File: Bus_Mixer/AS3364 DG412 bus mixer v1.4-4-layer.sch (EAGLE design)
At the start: 139 parts, among them IC1 PCA9539PW, IC10 DG412-J, IC11 DG412-J, IC2 TL074JT, IC3 TL072JT, IC4 TL074JT, IC6 TL072JT, IC7 TL074JT, IC8 DG412-J, IC9 DG412-J

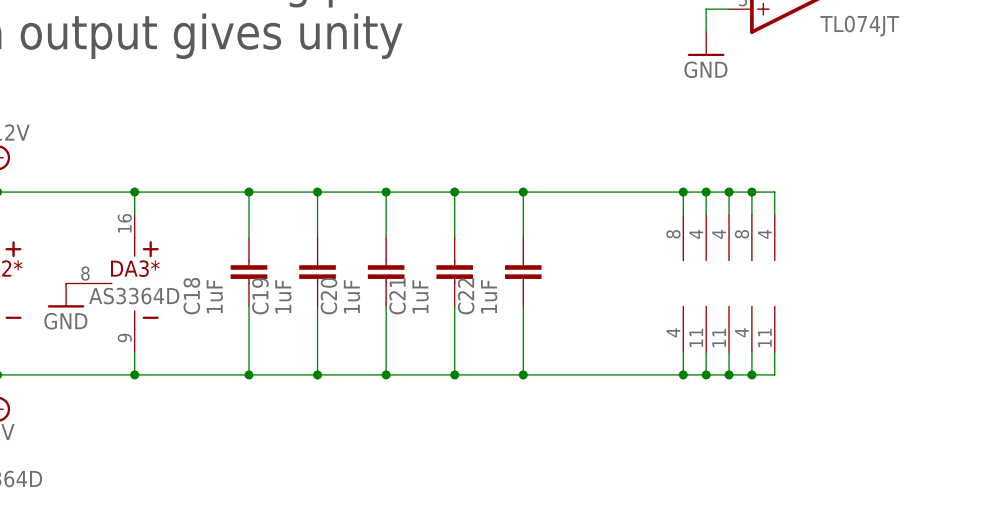
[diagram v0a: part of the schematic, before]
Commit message: Added better decoupling caps
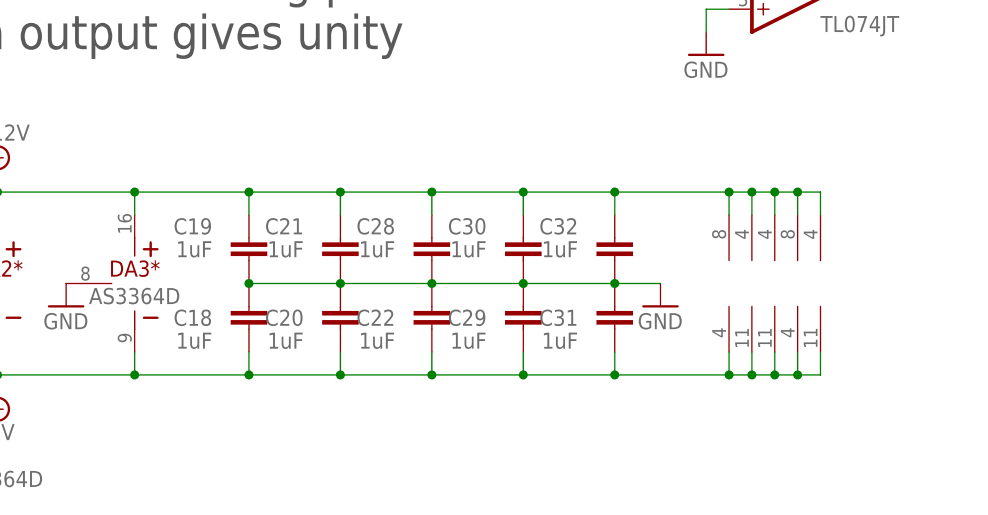
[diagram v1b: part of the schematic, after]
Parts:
- added C28, C29, C30, C31, C32: 1uF, joakim:C-EU-J0402
- C18, C19, C20, C21, C22, C23: device rcl:C-EUC0402 -> joakim:C-EU-J0402
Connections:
- net +12V: now also C28.2, C30.2, C32.2; no longer C18.2, C20.2, C22.2
- net -12V: now also C29.1, C31.1; no longer C19.1, C21.1
- net GND: now also C18.2, C19.1, C20.2, C21.1, C22.2, C28.1, C29.2, C30.1, C31.2, C32.1
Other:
- moved on the sheet: C18, C19, C20, C21, C22

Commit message: Routed chain inverter
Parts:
- added JP1: JUMPER-SMT_2_NC_TRACE_SILK-DNM, SparkFun-Jumpers:JUMPER-SMT_2_NC_TRACE_SILK
- added JP4: JUMPER-SMT_2_NO_SILK-DNM, SparkFun-Jumpers:JUMPER-SMT_2_NO_SILK
- added R98, R99: 47k, rcl:R-EU_R0402
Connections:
- new net N$44: IC7A.-IN, R98.2, R99.1
- new net SVF_CHAIN_SELECTED: JP1.2, JP4.2, R69.2
- net N$22: now also JP4.1, R98.1; no longer IC7A.-IN
- net SVF_CHAIN: now also JP1.1, R99.2; no longer R69.2
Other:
- note added: "SVF chain phase fuckup protection"
- note removed: "INs are 47k summing points. 47k on output gives unity gain"
- note removed: "TODO: Bruke opamp 2 til å invertere DRY A?"
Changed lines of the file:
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@@
 <part name="C32" library="joakim" deviceset="C-EU-J" device="0402" value="1uF"/>
 <part name="GND44" library="supply1" library_urn="urn:adsk.eagle:library:371" deviceset="GND" device=""/>
+<part name="JP1" library="SparkFun-Jumpers" library_urn="urn:adsk.eagle:library:528" deviceset="JUMPER-SMT_2_NC_TRACE" device="_SILK" package3d_urn="urn:adsk.eagle:package:39281/2" value="JUMPER-SMT_2_NC_TRACE_SILK-DNM"/>
+<part name="JP4" library="SparkFun-Jumpers" library_urn="urn:adsk.eagle:library:528" deviceset="JUMPER-SMT_2_NO" device="_SILK" package3d_urn="urn:adsk.eagle:package:39279/1" value="JUMPER-SMT_2_NO_SILK-DNM"/>
+<part name="R98" library="rcl" library_urn="urn:adsk.eagle:library:334" deviceset="R-EU_" device="R0402" package3d_urn="urn:adsk.eagle:package:23547/3" value="47k"/>
+<part name="R99" library="rcl" library_urn="urn:adsk.eagle:library:334" deviceset="R-EU_" device="R0402" package3d_urn="urn:adsk.eagle:package:23547/3" value="47k"/>
 </parts>
 <sheets>
 <sheet>
 <plain>
-<text x="33.02" y="-147.32" size="3.81" layer="97">INs are 47k summing points.
-47k on output gives unity
-gain</text>
+<text x="162.56" y="-124.46" size="3.81" layer="97">SVF chain phase
+fuckup protection</text>
 <text x="246.38" y="69.85" size="1.778" layer="97">Modules</text>
 <text x="247.65" y="63.5" size="1.778" layer="97">5V</text>
@@
 <text x="-7.62" y="12.7" size="1.778" layer="97">Add to increase
 gain for noise</text>
-<text x="116.84" y="-119.38" size="1.778" layer="91">TODO: Bruke opamp 2 til å invertere
-DRY A?</text>
 </plain>
 <instances>
@@
 <attribute name="VALUE" x="119.38" y="-172.72" size="1.778" layer="96"/>
 </instance>
+<instance part="JP1" gate="G$1" x="152.4" y="-119.38" smashed="yes">
+<attribute name="NAME" x="152.4" y="-116.332" size="1.778" layer="95" font="vector" align="center"/>
+</instance>
+<instance part="JP4" gate="G$1" x="152.4" y="-134.62" smashed="yes">
+<attribute name="NAME" x="152.4" y="-131.826" size="1.778" layer="95" font="vector" align="center"/>
+</instance>
+<instance part="R98" gate="G$1" x="137.16" y="-124.46" smashed="yes" rot="R180">
+<attribute name="NAME" x="140.97" y="-125.9586" size="1.778" layer="95" rot="R180"/>
+<attribute name="VALUE" x="140.97" y="-121.158" size="1.778" layer="96" rot="R180"/>
+</instance>
+<instance part="R99" gate="G$1" x="119.38" y="-132.08" smashed="yes" rot="R180">
+<attribute name="NAME" x="123.19" y="-133.5786" size="1.778" layer="95" rot="R180"/>
+<attribute name="VALUE" x="123.19" y="-128.778" size="1.778" layer="96" rot="R180"/>
+</instance>
 </instances>
 <busses>
@@
 <net name="SVF_CHAIN" class="0">
 <segment>
-<pinref part="R69" gate="G$1" pin="2"/>
-<wire x1="88.9" y1="-63.5" x2="63.5" y2="-63.5" width="0.1524" layer="91"/>
-<label x="63.5" y="-63.5" size="1.778" layer="95"/>
-</segment>
-<segment>
 <wire x1="-91.44" y1="-2.54" x2="-66.04" y2="-2.54" width="0.1524" layer="91"/>
 <label x="-88.9" y="-2.54" size="1.778" layer="95"/>
 <pinref part="U$3" gate="G$1" pin="16"/>
 </segment>
+<segment>
+<pinref part="JP1" gate="G$1" pin="1"/>
+<wire x1="147.32" y1="-119.38" x2="114.3" y2="-119.38" width="0.1524" layer="91"/>
+<pinref part="R99" gate="G$1" pin="2"/>
+<wire x1="114.3" y1="-132.08" x2="104.14" y2="-132.08" width="0.1524" layer="91"/>
+<wire x1="114.3" y1="-132.08" x2="114.3" y2="-119.38" width="0.1524" layer="91"/>
+<junction x="114.3" y="-132.08"/>
+<label x="99.06" y="-132.08" size="1.778" layer="95"/>
+</segment>
 </net>
 <net name="N$20" class="0">
@@
 <net name="N$22" class="0">
 <segment>
-<wire x1="129.54" y1="-132.08" x2="127" y2="-132.08" width="0.1524" layer="91"/>
-<wire x1="127" y1="-132.08" x2="127" y2="-127" width="0.1524" layer="91"/>
-<wire x1="127" y1="-127" x2="147.32" y2="-127" width="0.1524" layer="91"/>
-<wire x1="147.32" y1="-127" x2="147.32" y2="-134.62" width="0.1524" layer="91"/>
+<wire x1="147.32" y1="-124.46" x2="147.32" y2="-134.62" width="0.1524" layer="91"/>
 <wire x1="147.32" y1="-134.62" x2="144.78" y2="-134.62" width="0.1524" layer="91"/>
-<pinref part="IC7" gate="A" pin="-IN"/>
 <pinref part="IC7" gate="A" pin="OUT"/>
+<pinref part="JP4" gate="G$1" pin="1"/>
+<junction x="147.32" y="-134.62"/>
+<pinref part="R98" gate="G$1" pin="1"/>
+<wire x1="142.24" y1="-124.46" x2="147.32" y2="-124.46" width="0.1524" layer="91"/>
 </segment>
 </net>
@@
 </segment>
 </net>
+<net name="SVF_CHAIN_SELECTED" class="0">
+<segment>
+<pinref part="JP1" gate="G$1" pin="2"/>
+<pinref part="JP4" gate="G$1" pin="2"/>
+<wire x1="157.48" y1="-119.38" x2="157.48" y2="-134.62" width="0.1524" layer="91"/>
+<wire x1="157.48" y1="-134.62" x2="170.18" y2="-134.62" width="0.1524" layer="91"/>
+<junction x="157.48" y="-134.62"/>
+<label x="160.02" y="-134.62" size="1.778" layer="95"/>
+</segment>
+<segment>
+<pinref part="R69" gate="G$1" pin="2"/>
+<wire x1="88.9" y1="-63.5" x2="63.5" y2="-63.5" width="0.1524" layer="91"/>
+<label x="63.5" y="-63.5" size="1.778" layer="95"/>
+</segment>
+</net>
+<net name="N$44" class="0">
+<segment>
+<pinref part="R98" gate="G$1" pin="2"/>
+<pinref part="IC7" gate="A" pin="-IN"/>
+<wire x1="129.54" y1="-132.08" x2="127" y2="-132.08" width="0.1524" layer="91"/>
+<pinref part="R99" gate="G$1" pin="1"/>
+<wire x1="124.46" y1="-132.08" x2="127" y2="-132.08" width="0.1524" layer="91"/>
+<junction x="127" y="-132.08"/>
+<wire x1="127" y1="-132.08" x2="127" y2="-124.46" width="0.1524" layer="91"/>
+<wire x1="127" y1="-124.46" x2="132.08" y2="-124.46" width="0.1524" layer="91"/>
+</segment>
+</net>
